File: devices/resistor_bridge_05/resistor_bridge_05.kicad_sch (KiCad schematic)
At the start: 9 parts

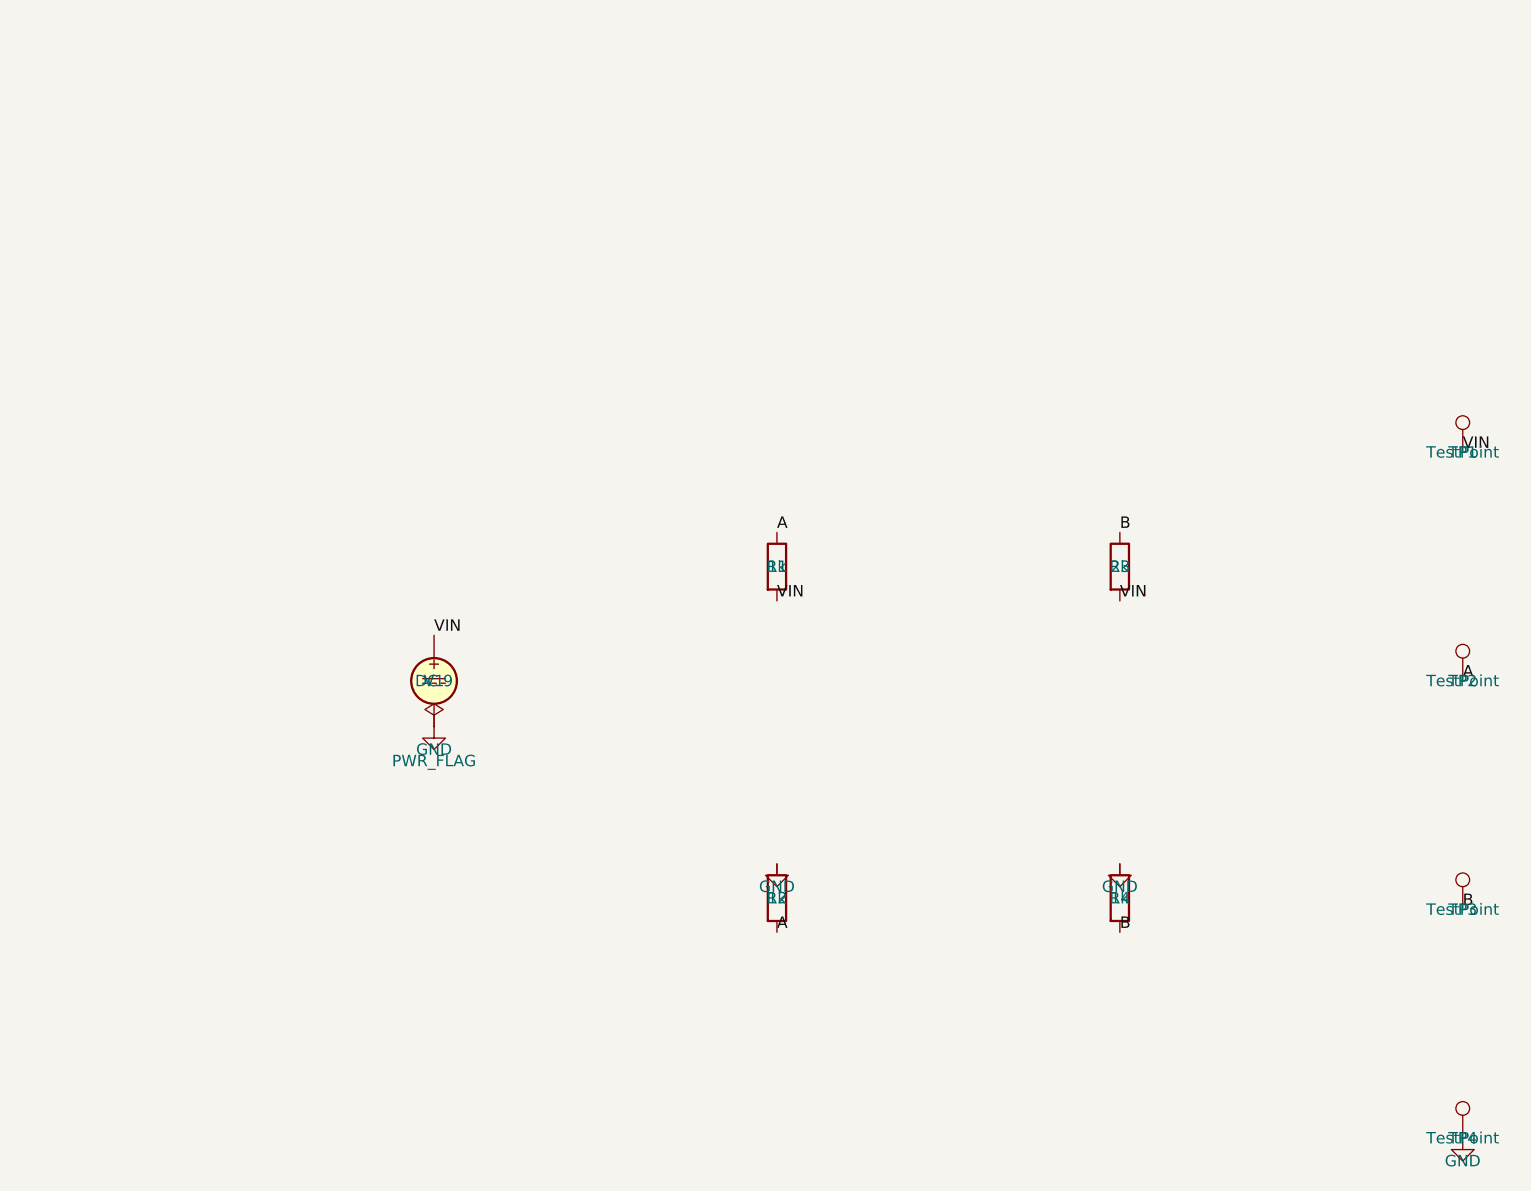
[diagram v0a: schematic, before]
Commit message: Schematics: draw real wires between components, not just net labels
Confirmed the diagnosis before touching anything: every device's .kicad_sch
had zero (wire ...) elements -- connectivity was entirely via same-named
net labels (which KiCad does merge into one net sheet-wide with no wire
between them, confirmed empirically). Correct for simulation/netlist
purposes, but the schematic view rendered as scattered disconnected
symbols with floating TP markers -- not because of a KiCanvas rendering
gap, but because there was genuinely no wire geometry in the source.

Rebuilds all 5 devices with real (wire ...) segments and (junction ...)
dots connecting every pin, and repositions each TP marker to tap directly
off its wire instead of floating in its own column. Also switches every
device from a full A4 sheet to a compact page sized to its own circuit
(kicadCoords.ts's schematicMmToPixels updated to match) -- on A4 the
actual symbols were tiny relative to the fixed-size TP marker overlay;
sized to content, the same symbols occupy far more of the viewport.

Two real routing bugs found and fixed via ERC + a real exported netlist
at every step (not just "0 ERC errors", which doesn't catch either of
these):
- diode_indicator_03: two different nets' horizontal wire runs shared the
  same Y with overlapping X ranges -- collinear overlap merges wires into
  one net, same as overlapping copper would, silently folding GND and N1
  together.
- resistor_bridge_05: a tap wire spanned past a component's *other* pin
  along the same column (a pin lying anywhere along a wire's path counts
  as connected, not just at a declared endpoint) -- collapsed every net
  into one. Also separately found: two adjacent TP markers ended up only
  3.81mm apart, too close for the existing 44px mobile tap target to not
  overlap -- widened that specific gap.

Verified end-to-end after deploying: every device re-imported through the
real API, full backend+frontend suites green, and a live-browser sweep of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
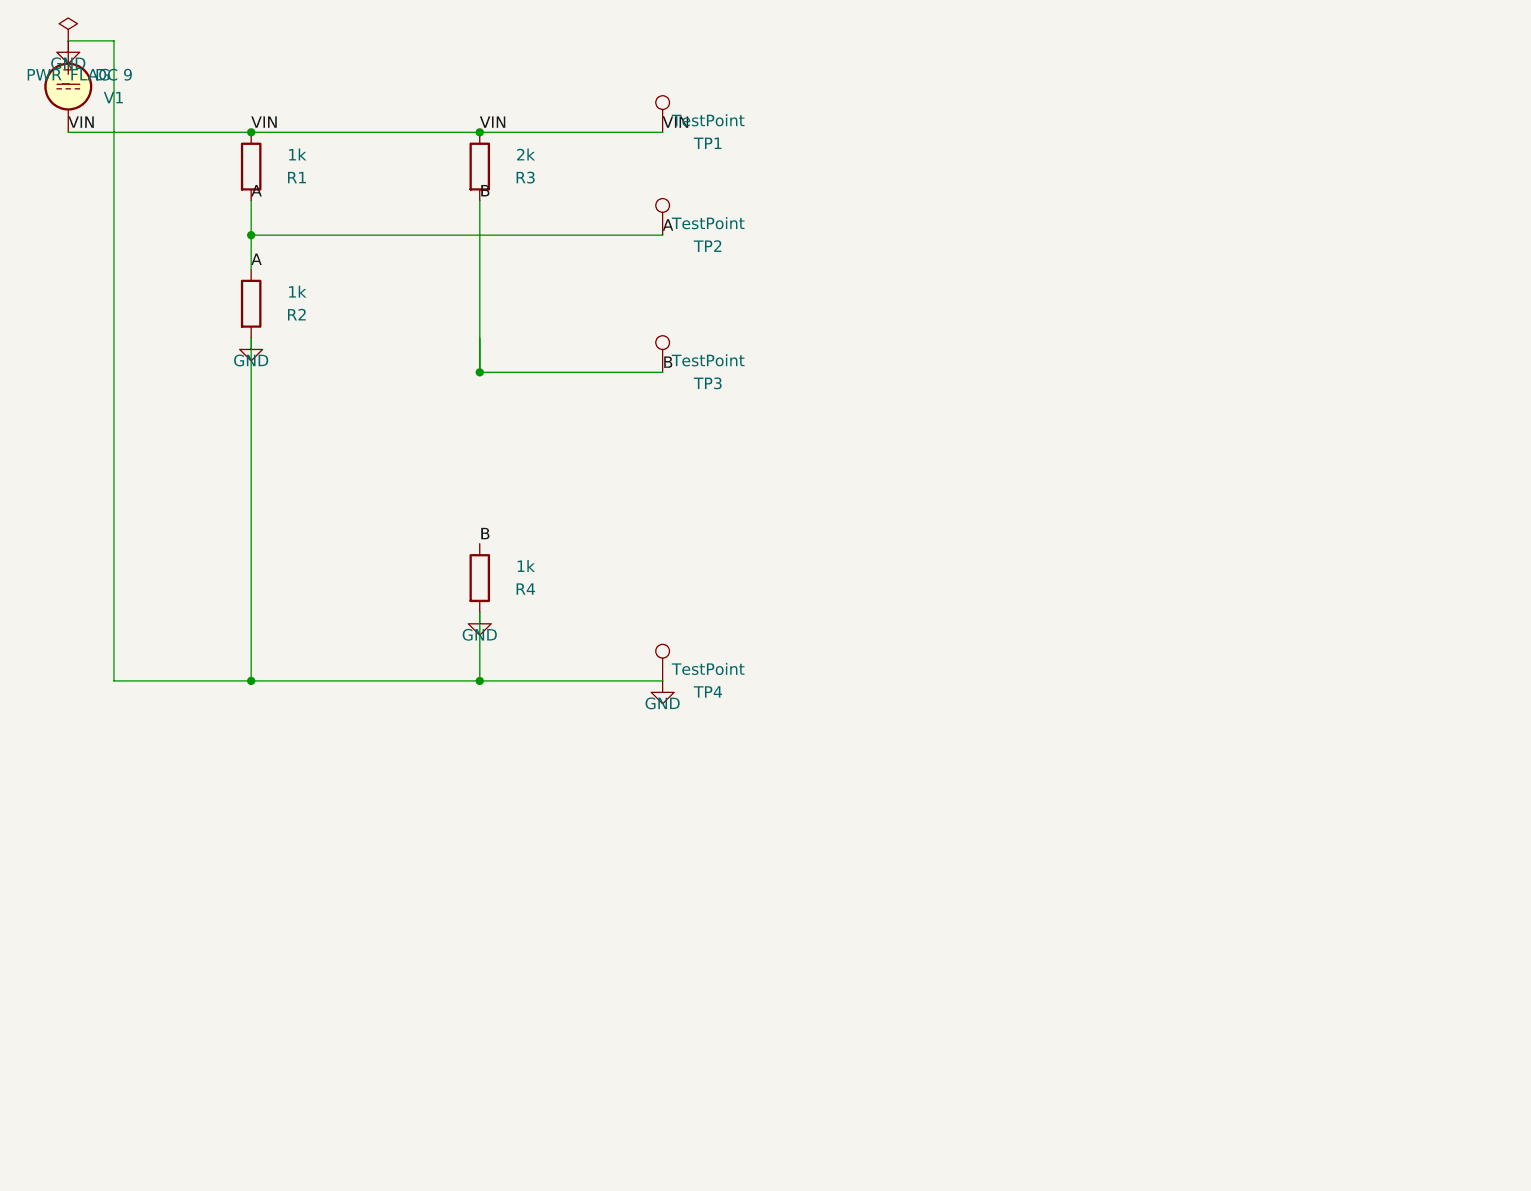
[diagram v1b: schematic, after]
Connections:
- net A: now also R1.2, R2.1; no longer R1.1, R2.2
- net B: now also R3.2, R4.1; no longer R3.1, R4.2
- net GND: now also R2.2, R4.2, V1.1; no longer R2.1, R4.1, V1.2
- net VIN: now also R1.1, R3.1, V1.2; no longer R1.2, R3.2, V1.1
